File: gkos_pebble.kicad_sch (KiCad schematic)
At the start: 26 parts, among them J1 10129383-906002BLF

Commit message: reannotate
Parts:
- renumbered TP16 to TP14, TP17 to TP15, TP18 to TP16, TP19 to TP17, TP20 to TP18, TP21 to TP19, TP22 to TP20, TP23 to TP21, TP24 to TP22, TP25 to TP23, TP26 to TP24, TP27 to TP25

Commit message: in progress pcb
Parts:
- TP1, TP10, TP11, TP12, TP13, TP14, TP15, TP16, TP17, TP18, TP19, TP2, TP20, TP21, TP22, TP23, TP24, TP25, TP3, TP4, TP5, TP6, TP7, TP8, TP9: footprint TestPoint:TestPoint_Pad_D2.0mm -> TestPoint:TestPoint_Pad_D1.0mm
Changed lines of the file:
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@@
       (effects (font (size 1.27 1.27)) (justify left))
     )
-    (property "Footprint" "TestPoint:TestPoint_Pad_D2.0mm" (at 157.48 130.81 0)
+    (property "Footprint" "TestPoint:TestPoint_Pad_D1.0mm" (at 157.48 130.81 0)
       (effects (font (size 1.27 1.27)) hide)
     )
@@
       (effects (font (size 1.27 1.27)) (justify left))
     )
-    (property "Footprint" "TestPoint:TestPoint_Pad_D2.0mm" (at 93.98 92.71 0)
+    (property "Footprint" "TestPoint:TestPoint_Pad_D1.0mm" (at 93.98 92.71 0)
       (effects (font (size 1.27 1.27)) hide)
     )
@@
       (effects (font (size 1.27 1.27)) (justify left))
     )
-    (property "Footprint" "TestPoint:TestPoint_Pad_D2.0mm" (at 114.3 130.81 0)
+    (property "Footprint" "TestPoint:TestPoint_Pad_D1.0mm" (at 114.3 130.81 0)
       (effects (font (size 1.27 1.27)) hide)
     )
@@
       (effects (font (size 1.27 1.27)) (justify left))
     )
-    (property "Footprint" "TestPoint:TestPoint_Pad_D2.0mm" (at 153.67 62.23 0)
+    (property "Footprint" "TestPoint:TestPoint_Pad_D1.0mm" (at 153.67 62.23 0)
       (effects (font (size 1.27 1.27)) hide)
     )
@@
       (effects (font (size 1.27 1.27)) (justify left))
     )
-    (property "Footprint" "TestPoint:TestPoint_Pad_D2.0mm" (at 93.98 118.11 0)
+    (property "Footprint" "TestPoint:TestPoint_Pad_D1.0mm" (at 93.98 118.11 0)
       (effects (font (size 1.27 1.27)) hide)
     )
@@
       (effects (font (size 1.27 1.27)) (justify left))
     )
-    (property "Footprint" "TestPoint:TestPoint_Pad_D2.0mm" (at 93.98 113.03 0)
+    (property "Footprint" "TestPoint:TestPoint_Pad_D1.0mm" (at 93.98 113.03 0)
       (effects (font (size 1.27 1.27)) hide)
     )
@@
       (effects (font (size 1.27 1.27)) (justify left))
     )
-    (property "Footprint" "TestPoint:TestPoint_Pad_D2.0mm" (at 157.48 113.03 0)
+    (property "Footprint" "TestPoint:TestPoint_Pad_D1.0mm" (at 157.48 113.03 0)
       (effects (font (size 1.27 1.27)) hide)
     )
@@
       (effects (font (size 1.27 1.27)) (justify left))
     )
-    (property "Footprint" "TestPoint:TestPoint_Pad_D2.0mm" (at 114.3 123.19 0)
+    (property "Footprint" "TestPoint:TestPoint_Pad_D1.0mm" (at 114.3 123.19 0)
       (effects (font (size 1.27 1.27)) hide)
     )
@@
       (effects (font (size 1.27 1.27)) (justify left))
     )
-    (property "Footprint" "TestPoint:TestPoint_Pad_D2.0mm" (at 157.48 105.41 0)
+    (property "Footprint" "TestPoint:TestPoint_Pad_D1.0mm" (at 157.48 105.41 0)
       (effects (font (size 1.27 1.27)) hide)
     )
@@
       (effects (font (size 1.27 1.27)) (justify left))
     )
-    (property "Footprint" "TestPoint:TestPoint_Pad_D2.0mm" (at 157.48 133.35 0)
+    (property "Footprint" "TestPoint:TestPoint_Pad_D1.0mm" (at 157.48 133.35 0)
       (effects (font (size 1.27 1.27)) hide)
     )
@@
       (effects (font (size 1.27 1.27)) (justify left))
     )
-    (property "Footprint" "TestPoint:TestPoint_Pad_D2.0mm" (at 93.98 95.25 0)
+    (property "Footprint" "TestPoint:TestPoint_Pad_D1.0mm" (at 93.98 95.25 0)
       (effects (font (size 1.27 1.27)) hide)
     )
@@
       (effects (font (size 1.27 1.27)) (justify left))
     )
-    (property "Footprint" "TestPoint:TestPoint_Pad_D2.0mm" (at 93.98 74.93 0)
+    (property "Footprint" "TestPoint:TestPoint_Pad_D1.0mm" (at 93.98 74.93 0)
       (effects (font (size 1.27 1.27)) hide)
     )
@@
       (effects (font (size 1.27 1.27)) (justify left))
     )
-    (property "Footprint" "TestPoint:TestPoint_Pad_D2.0mm" (at 93.98 97.79 0)
+    (property "Footprint" "TestPoint:TestPoint_Pad_D1.0mm" (at 93.98 97.79 0)
       (effects (font (size 1.27 1.27)) hide)
     )
@@
       (effects (font (size 1.27 1.27)) (justify left))
     )
-    (property "Footprint" "TestPoint:TestPoint_Pad_D2.0mm" (at 114.3 133.35 0)
+    (property "Footprint" "TestPoint:TestPoint_Pad_D1.0mm" (at 114.3 133.35 0)
       (effects (font (size 1.27 1.27)) hide)
     )
@@
       (effects (font (size 1.27 1.27)) (justify left))
     )
-    (property "Footprint" "TestPoint:TestPoint_Pad_D2.0mm" (at 93.98 100.33 0)
+    (property "Footprint" "TestPoint:TestPoint_Pad_D1.0mm" (at 93.98 100.33 0)
       (effects (font (size 1.27 1.27)) hide)
     )
@@
       (effects (font (size 1.27 1.27)) (justify left))
     )
-    (property "Footprint" "TestPoint:TestPoint_Pad_D2.0mm" (at 93.98 105.41 0)
+    (property "Footprint" "TestPoint:TestPoint_Pad_D1.0mm" (at 93.98 105.41 0)
       (effects (font (size 1.27 1.27)) hide)
     )
@@
       (effects (font (size 1.27 1.27)) (justify left))
     )
-    (property "Footprint" "TestPoint:TestPoint_Pad_D2.0mm" (at 157.48 107.95 0)
+    (property "Footprint" "TestPoint:TestPoint_Pad_D1.0mm" (at 157.48 107.95 0)
       (effects (font (size 1.27 1.27)) hide)
     )
@@
       (effects (font (size 1.27 1.27)) (justify left))
     )
-    (property "Footprint" "TestPoint:TestPoint_Pad_D2.0mm" (at 157.48 110.49 0)
+    (property "Footprint" "TestPoint:TestPoint_Pad_D1.0mm" (at 157.48 110.49 0)
       (effects (font (size 1.27 1.27)) hide)
     )
@@
       (effects (font (size 1.27 1.27)) (justify left))
     )
-    (property "Footprint" "TestPoint:TestPoint_Pad_D2.0mm" (at 93.98 62.23 0)
+    (property "Footprint" "TestPoint:TestPoint_Pad_D1.0mm" (at 93.98 62.23 0)
       (effects (font (size 1.27 1.27)) hide)
     )
@@
       (effects (font (size 1.27 1.27)) (justify left))
     )
-    (property "Footprint" "TestPoint:TestPoint_Pad_D2.0mm" (at 93.98 77.47 0)
+    (property "Footprint" "TestPoint:TestPoint_Pad_D1.0mm" (at 93.98 77.47 0)
       (effects (font (size 1.27 1.27)) hide)
     )
@@
       (effects (font (size 1.27 1.27)) (justify left))
     )
-    (property "Footprint" "TestPoint:TestPoint_Pad_D2.0mm" (at 93.98 115.57 0)
+    (property "Footprint" "TestPoint:TestPoint_Pad_D1.0mm" (at 93.98 115.57 0)
       (effects (font (size 1.27 1.27)) hide)
     )
@@
       (effects (font (size 1.27 1.27)) (justify left))
     )
-    (property "Footprint" "TestPoint:TestPoint_Pad_D2.0mm" (at 153.67 64.77 0)
+    (property "Footprint" "TestPoint:TestPoint_Pad_D1.0mm" (at 153.67 64.77 0)
       (effects (font (size 1.27 1.27)) hide)
     )
@@
       (effects (font (size 1.27 1.27)) (justify left))
     )
-    (property "Footprint" "TestPoint:TestPoint_Pad_D2.0mm" (at 114.3 125.73 0)
+    (property "Footprint" "TestPoint:TestPoint_Pad_D1.0mm" (at 114.3 125.73 0)
       (effects (font (size 1.27 1.27)) hide)
     )
@@
       (effects (font (size 1.27 1.27)) (justify left))
     )
-    (property "Footprint" "TestPoint:TestPoint_Pad_D2.0mm" (at 93.98 110.49 0)
+    (property "Footprint" "TestPoint:TestPoint_Pad_D1.0mm" (at 93.98 110.49 0)
       (effects (font (size 1.27 1.27)) hide)
     )
@@
       (effects (font (size 1.27 1.27)) (justify left))
     )
-    (property "Footprint" "TestPoint:TestPoint_Pad_D2.0mm" (at 93.98 102.87 0)
-      (effects (font (size 1.27 1.27)) hide)
-    )
+    (property "Footprint" "TestPoint:TestPoint_Pad_D1.0mm" (at 93.98 102.87 0)
+      (effects (font (size 1.27 1.27)) hide)
+    )

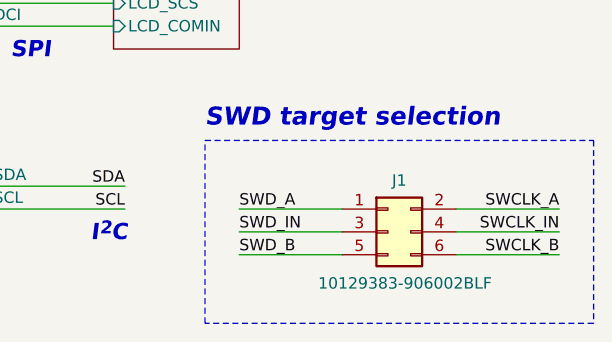
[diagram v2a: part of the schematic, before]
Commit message: change 2.54mm SWD header to 1.27mm
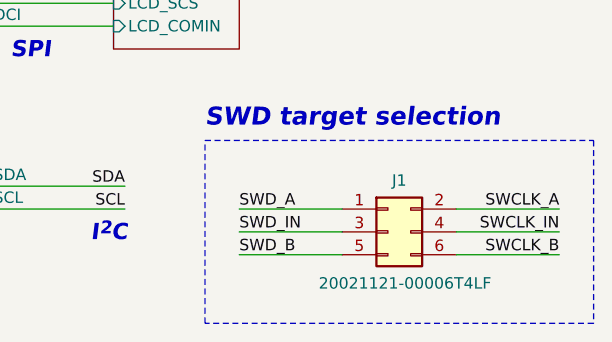
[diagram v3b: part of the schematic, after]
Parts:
- J1: value 10129383-906002BLF -> 20021121-00006T4LF; footprint Connector_PinHeader_2.54mm:PinHeader_2x03_P2.54mm_Vertical_SMD -> Connector_PinHeader_1.27mm:PinHeader_2x03_P1.27mm_Vertical_SMD
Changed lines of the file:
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@@
       (effects (font (size 1.27 1.27)))
     )
-    (property "Value" "10129383-906002BLF" (at 198.755 141.605 0)
+    (property "Value" "20021121-00006T4LF" (at 198.755 141.605 0)
       (effects (font (size 1.27 1.27)))
     )
-    (property "Footprint" "Connector_PinHeader_2.54mm:PinHeader_2x03_P2.54mm_Vertical_SMD" (at 196.85 135.89 0)
+    (property "Footprint" "Connector_PinHeader_1.27mm:PinHeader_2x03_P1.27mm_Vertical_SMD" (at 196.85 135.89 0)
       (effects (font (size 1.27 1.27)) hide)
     )

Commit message: in-progress second layout attempt
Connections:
- net SWCLK_A: now also J1.1 (Pin_1); no longer J1.2 (Pin_2)
- net SWCLK_B: now also J1.5 (Pin_5); no longer J1.6 (Pin_6)
- net SWCLK_IN: now also J1.3 (Pin_3); no longer J1.4 (Pin_4)
- net SWD_A: now also J1.2 (Pin_2); no longer J1.1 (Pin_1)
- net SWD_B: now also J1.6 (Pin_6); no longer J1.5 (Pin_5)
- net SWD_IN: now also J1.4 (Pin_4); no longer J1.3 (Pin_3)

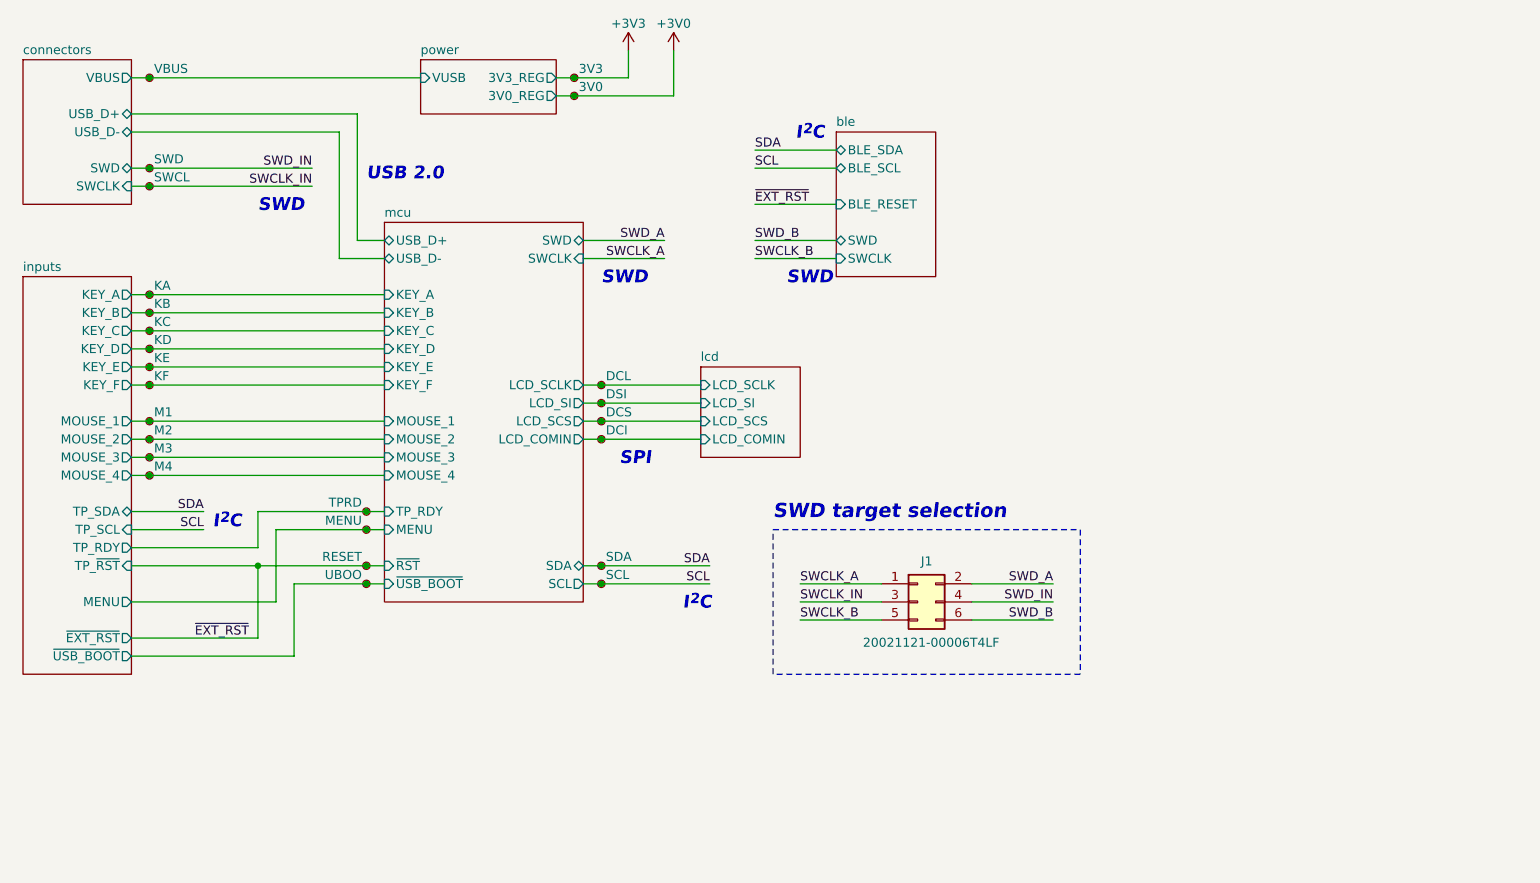
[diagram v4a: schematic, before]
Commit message: pcb done, also kicad 8
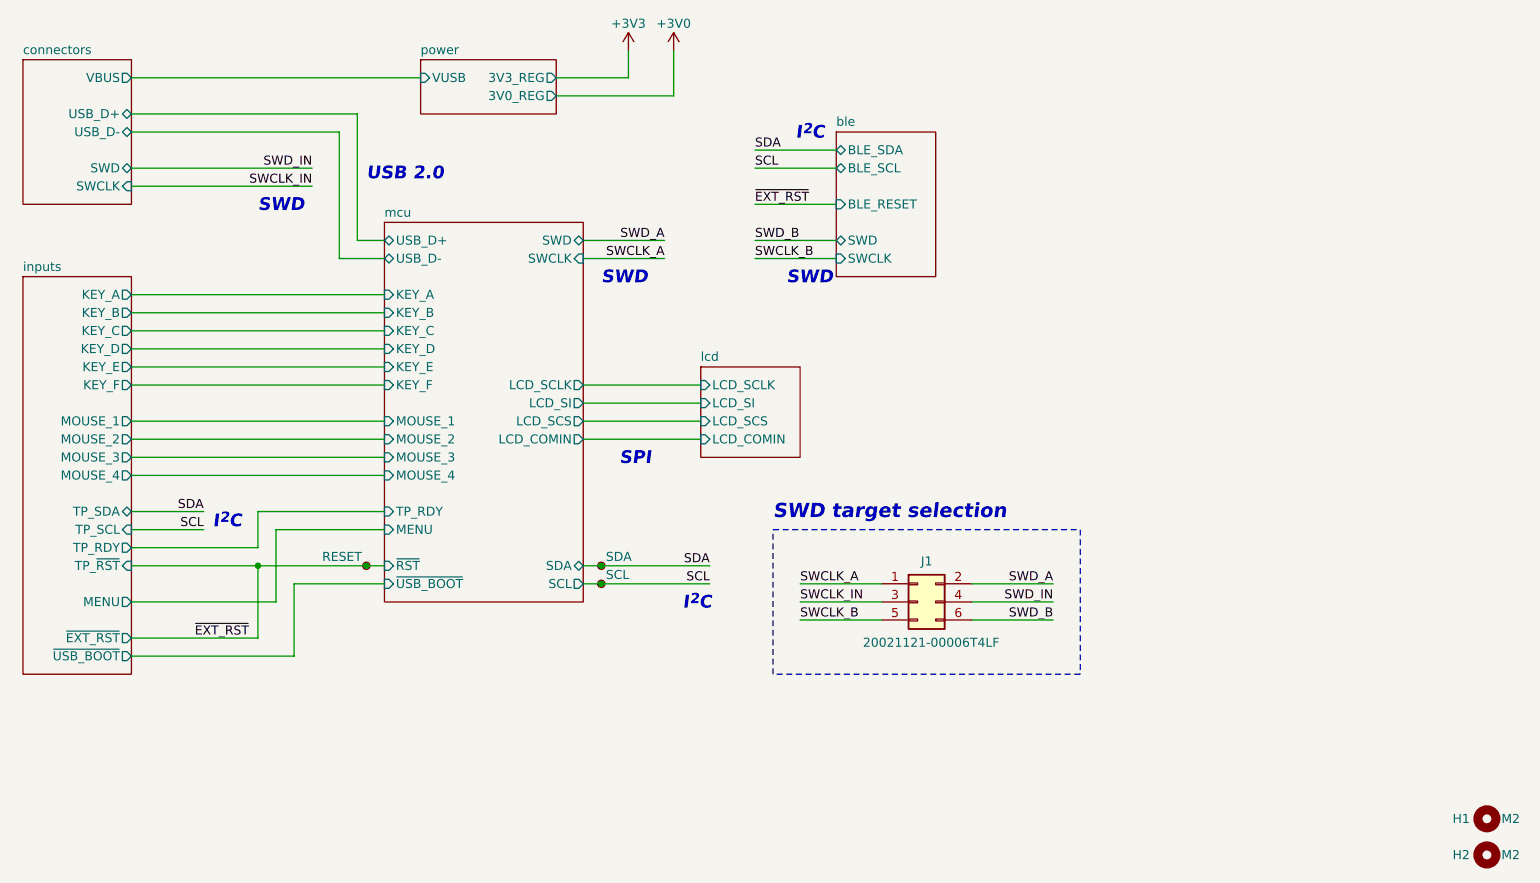
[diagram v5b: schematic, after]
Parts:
- removed TP1: VBUS, TestPoint:TestPoint_Pad_D1.0mm, symbol Connector:TestPoint_Small
- removed TP10: M1, TestPoint:TestPoint_Pad_D1.0mm, symbol Connector:TestPoint_Small
- removed TP11: M2, TestPoint:TestPoint_Pad_D1.0mm, symbol Connector:TestPoint_Small
- removed TP12: M3, TestPoint:TestPoint_Pad_D1.0mm, symbol Connector:TestPoint_Small
- removed TP13: M4, TestPoint:TestPoint_Pad_D1.0mm, symbol Connector:TestPoint_Small
- removed TP14: TPRD, TestPoint:TestPoint_Pad_D1.0mm, symbol Connector:TestPoint_Small
- removed TP15: MENU, TestPoint:TestPoint_Pad_D1.0mm, symbol Connector:TestPoint_Small
- removed TP17: UBOO, TestPoint:TestPoint_Pad_D1.0mm, symbol Connector:TestPoint_Small
- removed TP18: 3V3, TestPoint:TestPoint_Pad_D1.0mm, symbol Connector:TestPoint_Small
- removed TP19: 3V0, TestPoint:TestPoint_Pad_D1.0mm, symbol Connector:TestPoint_Small
- removed TP2: SWD, TestPoint:TestPoint_Pad_D1.0mm, symbol Connector:TestPoint_Small
- removed TP20: DCL, TestPoint:TestPoint_Pad_D1.0mm, symbol Connector:TestPoint_Small
- removed TP21: DSI, TestPoint:TestPoint_Pad_D1.0mm, symbol Connector:TestPoint_Small
- removed TP22: DCS, TestPoint:TestPoint_Pad_D1.0mm, symbol Connector:TestPoint_Small
- removed TP23: DCI, TestPoint:TestPoint_Pad_D1.0mm, symbol Connector:TestPoint_Small
- removed TP3: SWCL, TestPoint:TestPoint_Pad_D1.0mm, symbol Connector:TestPoint_Small
- removed TP4: KA, TestPoint:TestPoint_Pad_D1.0mm, symbol Connector:TestPoint_Small
- removed TP5: KB, TestPoint:TestPoint_Pad_D1.0mm, symbol Connector:TestPoint_Small
- removed TP6: KC, TestPoint:TestPoint_Pad_D1.0mm, symbol Connector:TestPoint_Small
- removed TP7: KD, TestPoint:TestPoint_Pad_D1.0mm, symbol Connector:TestPoint_Small
- removed TP8: KE, TestPoint:TestPoint_Pad_D1.0mm, symbol Connector:TestPoint_Small
- removed TP9: KF, TestPoint:TestPoint_Pad_D1.0mm, symbol Connector:TestPoint_Small
- added H1, H2: M2, MountingHole:MountingHole_2.2mm_M2, symbol Mechanical:MountingHole
- renumbered TP16 to TP1, TP24 to TP2, TP25 to TP3
